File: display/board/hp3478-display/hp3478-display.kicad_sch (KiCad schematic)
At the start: 2 parts, among them U1 PIC16F152xx-x_MP, U2 PIC16F152xx-x_PT

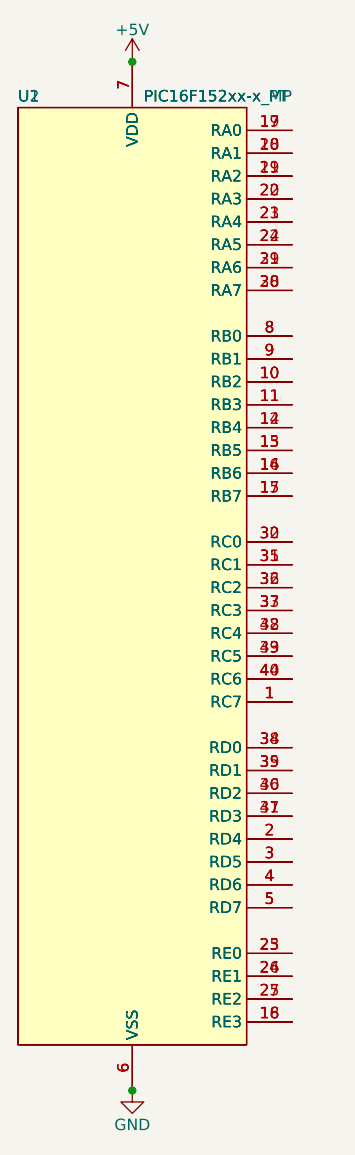
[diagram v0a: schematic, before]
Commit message: Clean up DNP alternate footprint for PIC.
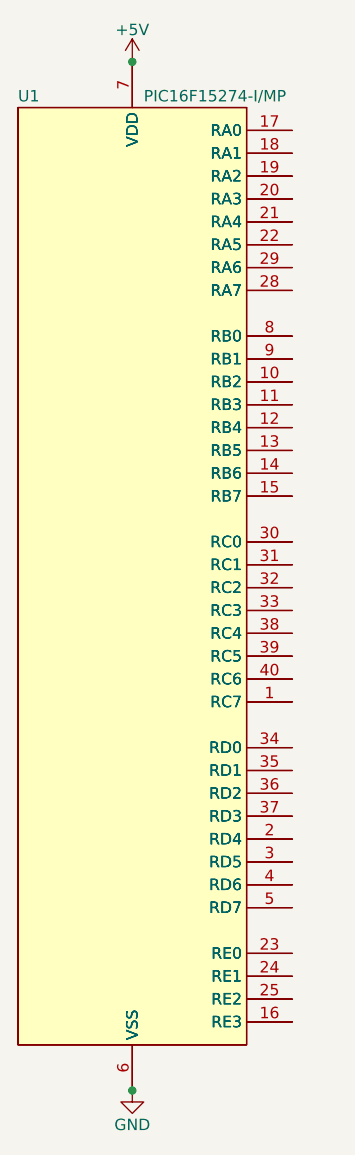
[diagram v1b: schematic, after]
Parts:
- U1: value PIC16F152xx-x_MP -> PIC16F15274-I/MP
- U2: value PIC16F152xx-x_PT -> DNP; now left out of the parts list
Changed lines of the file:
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@@
   )
   (symbol (lib_id "0Local:PIC16F152xx-x_PT") (at 40.64 130.81 0) (unit 1)
-    (in_bom yes) (on_board yes)
+    (in_bom no) (on_board yes)
     (property "Reference" "U2" (id 0) (at 27.94 83.82 0)
-      (effects (font (size 1.27 1.27)) (justify left))
+      (effects (font (size 1.27 1.27)) (justify left) hide)
     )
-    (property "Value" "PIC16F152xx-x_PT" (id 1) (at 41.91 83.82 0)
-      (effects (font (size 1.27 1.27)) (justify left))
+    (property "Value" "DNP" (id 1) (at 41.91 83.82 0)
+      (effects (font (size 1.27 1.27)) (justify left) hide)
     )
     (property "Footprint" "Package_QFP:TQFP-44_10x10mm_P0.8mm" (id 2) (at 40.64 130.81 0)
@@
       (effects (font (size 1.27 1.27)) (justify left))
     )
-    (property "Value" "PIC16F152xx-x_MP" (id 1) (at 41.91 83.82 0)
+    (property "Value" "PIC16F15274-I/MP" (id 1) (at 41.91 83.82 0)
       (effects (font (size 1.27 1.27)) (justify left))
     )
@@
     )
     (path "/84f97309-c012-475a-8346-a323e5986003"
-      (reference "U1") (unit 1) (value "PIC16F152xx-x_MP") (footprint "Package_DFN_QFN:QFN-40-1EP_5x5mm_P0.4mm_EP3.8x3.8mm_ThermalVias")
+      (reference "U1") (unit 1) (value "PIC16F15274-I/MP") (footprint "Package_DFN_QFN:QFN-40-1EP_5x5mm_P0.4mm_EP3.8x3.8mm_ThermalVias")
     )
     (path "/344cc245-2c6a-4a04-b559-c2e8c4d256b6"
-      (reference "U2") (unit 1) (value "PIC16F152xx-x_PT") (footprint "Package_QFP:TQFP-44_10x10mm_P0.8mm")
+      (reference "U2") (unit 1) (value "DNP") (footprint "Package_QFP:TQFP-44_10x10mm_P0.8mm")
     )
   )

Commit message: Assign all pins.
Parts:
- added C1: 22u, Capacitor_SMD:C_1206_3216Metric, symbol Device:C
- added C2, C3: 100n, Capacitor_SMD:C_0603_1608Metric, symbol Device:C
- added J1: SFV10R-1ST, 0Local:Amphenol_SFV10R-1ST, symbol Connector_Generic:Conn_01x10
- added J2: DNP, Connector_PinHeader_2.54mm:PinHeader_1x06_P2.54mm_Vertical, symbol Connector_Generic:Conn_01x06
- added R10, R11, R12, R13, R14, R15, R16, R17, R18, R19, R20, R21, R22, R23, R24, R25, R26: R, Resistor_SMD:R_0603_1608Metric, symbol Device:R
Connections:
- net +5V: now also C1.1, C2.1, C3.1, J1.1 (Pin_1), J1.2 (Pin_2), J2.2 (Pin_2)
- net GND: now also C1.2, C2.2, C3.2, J1.10 (Pin_10), J1.3 (Pin_3), J1.4 (Pin_4), J2.3 (Pin_3)
- net HA7: now reaches U1.1 (RC7), U2.1 (RC7)
- net HA7: now also R17.1
- net K8: now reaches U1.10 (RB2), U2.10 (RB2)
- net P1: now reaches U1.12 (RB4), U2.14 (RB4)
- net SYNC: now reaches U1.13 (RB5), U2.15 (RB5)
- net PGC/ISA: now reaches U1.14 (ICSPCLK/RB6), U2.16 (ICSPCLK/RB6)
- net PGC/ISA: now also J2.5 (Pin_5)
- net PGD/IWA: now reaches U1.15 (ICSPDAT/RB7), U2.17 (ICSPDAT/RB7)
- net PGD/IWA: now also J2.4 (Pin_4)
- net ~{MCLR}: now reaches U1.16 (~{MCLR}/RE3), U2.18 (~{MCLR}/RE3)
- net ~{MCLR}: now also J2.1 (Pin_1)
- net PWO: now reaches U1.17 (RA0), U2.19 (RA0)
- net HA12: now reaches U1.2 (RD4), U2.2 (RD4)
- net HA12: now also R22.1
- net K0: now reaches U1.18 (RA1), U2.20 (RA1)
- net K1: now reaches U1.19 (RA2), U2.21 (RA2)
- net K2: now reaches U1.20 (VREF/RA3), U2.22 (VREF/RA3)
- net K3: now reaches U1.21 (RA4), U2.23 (RA4)
- net K4: now reaches U1.22 (RA5), U2.24 (RA5)
- net K9: now reaches U1.23 (RE0), U2.25 (RE0)
- net K10: now reaches U1.24 (RE1), U2.26 (RE1)
- net K11: now reaches U1.25 (RE2), U2.27 (RE2)
- net HA13: now reaches U1.3 (RD5), U2.3 (RD5)
- net HA13: now also R23.1
- net K6: now reaches U1.28 (CLKIN/RA7), U2.30 (CLKIN/RA7)
- net K5: now reaches U1.29 (CLKOUT/RA6), U2.31 (CLKOUT/RA6)
- net HA0: now reaches U1.30 (RC0), U2.32 (RC0)
- net HA0: now also R10.1
- net HA1: now reaches U1.31 (RC1), U2.35 (RC1)
- net HA1: now also R11.1
- net HA2: now reaches U1.32 (RC2), U2.36 (RC2)
- net HA2: now also R12.1
- net HA3: now reaches U1.33 (RC3), U2.37 (RC3)
- net HA3: now also R13.1
- net HA8: now reaches U1.34 (RD0), U2.38 (RD0)
- net HA8: now also R18.1
- net HA9: now reaches U1.35 (RD1), U2.39 (RD1)
- net HA9: now also R19.1
- net HA14: now reaches U1.4 (RD6), U2.4 (RD6)
- net HA14: now also R24.1
- net HA10: now reaches U1.36 (RD2), U2.40 (RD2)
- net HA10: now also R20.1
- net HA11: now reaches U1.37 (RD3), U2.41 (RD3)
- net HA11: now also R21.1
- net HA4: now reaches U1.38 (RC4), U2.42 (RC4)
- net HA4: now also R14.1
- net HA5: now reaches U1.39 (RC5), U2.43 (RC5)
- net HA5: now also R15.1
- net HA6: now reaches U1.40 (RC6), U2.44 (RC6)
- net HA6: now also R16.1
- net HA15: now reaches U1.5 (RD7), U2.5 (RD7)
- net HA15: now also R25.1
- net HA16: now reaches U1.8 (RB0), U2.8 (RB0)
- net HA16: now also R26.1
- net K7: now reaches U1.9 (RB1), U2.9 (RB1)
- new net A0: R10.2
- new net A1: R11.2
- new net A10: R20.2
- new net A11: R21.2
- new net A12: R22.2
- new net A13: R23.2
- new net A14: R24.2
- new net A15: R25.2
- new net A16: R26.2
- new net A2: R12.2
- new net A3: R13.2
- new net A4: R14.2
- new net A5: R15.2
- new net A6: R16.2
- new net A7: R17.2
- new net A8: R18.2
- new net A9: R19.2
- no-connect marks 0 -> 1

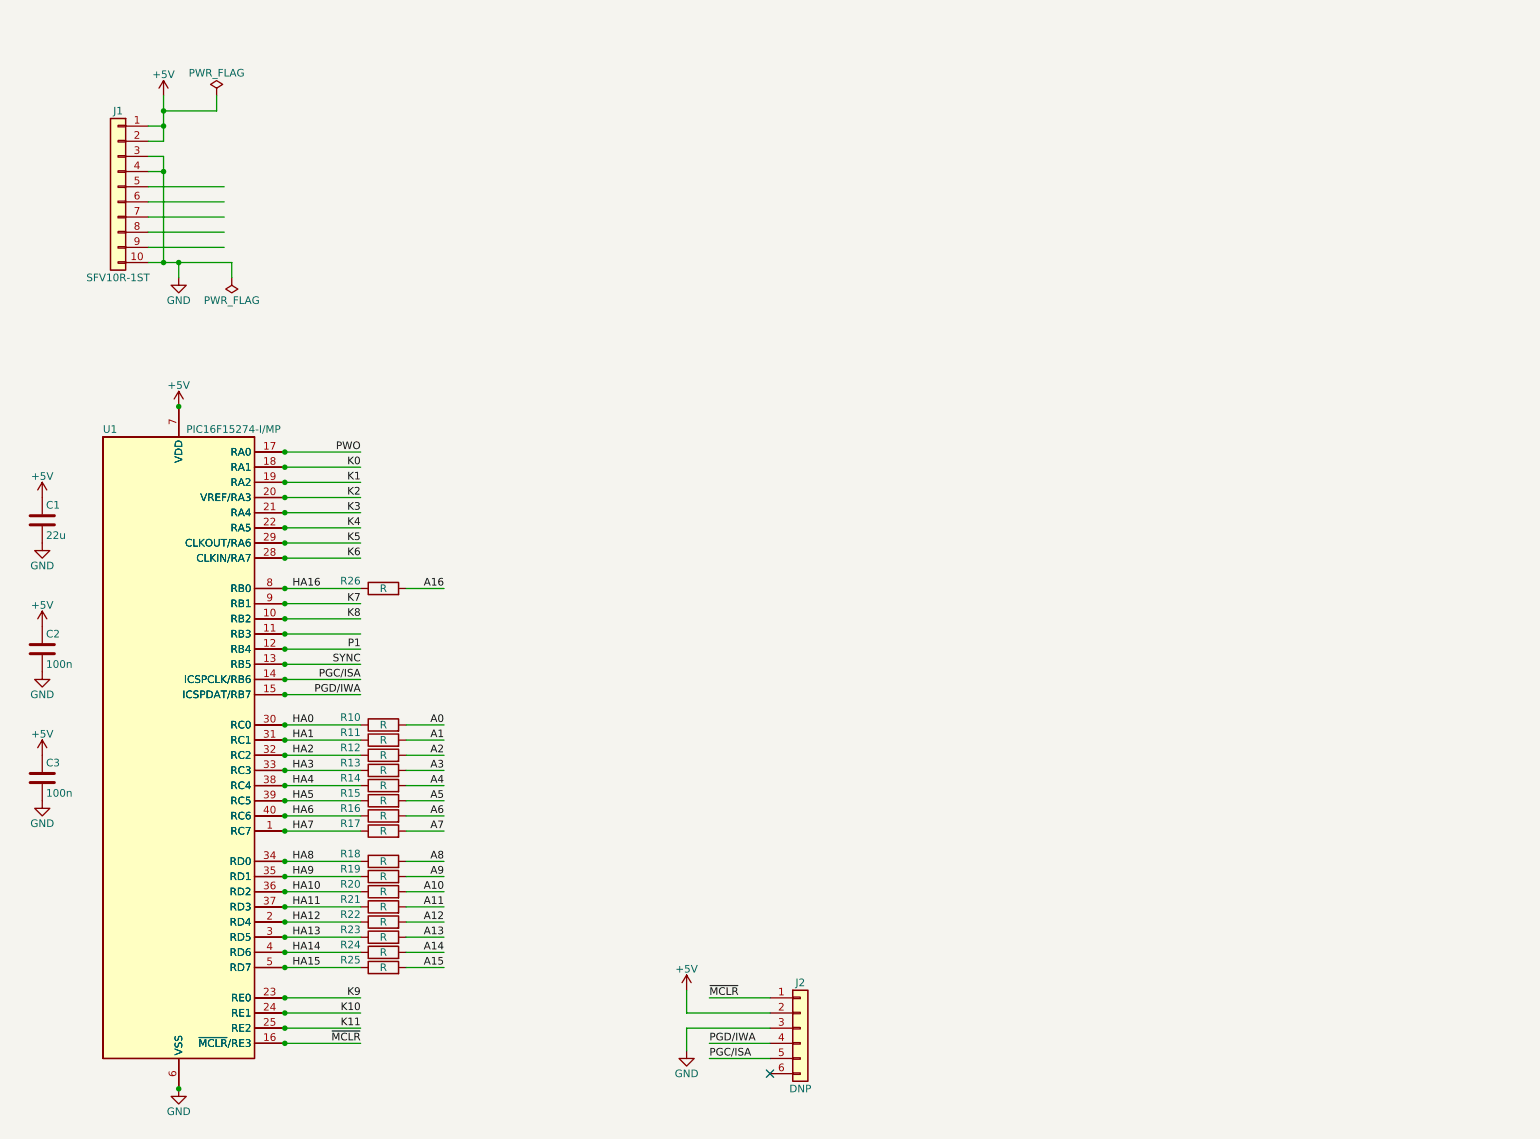
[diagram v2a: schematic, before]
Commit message: Add digits to board.
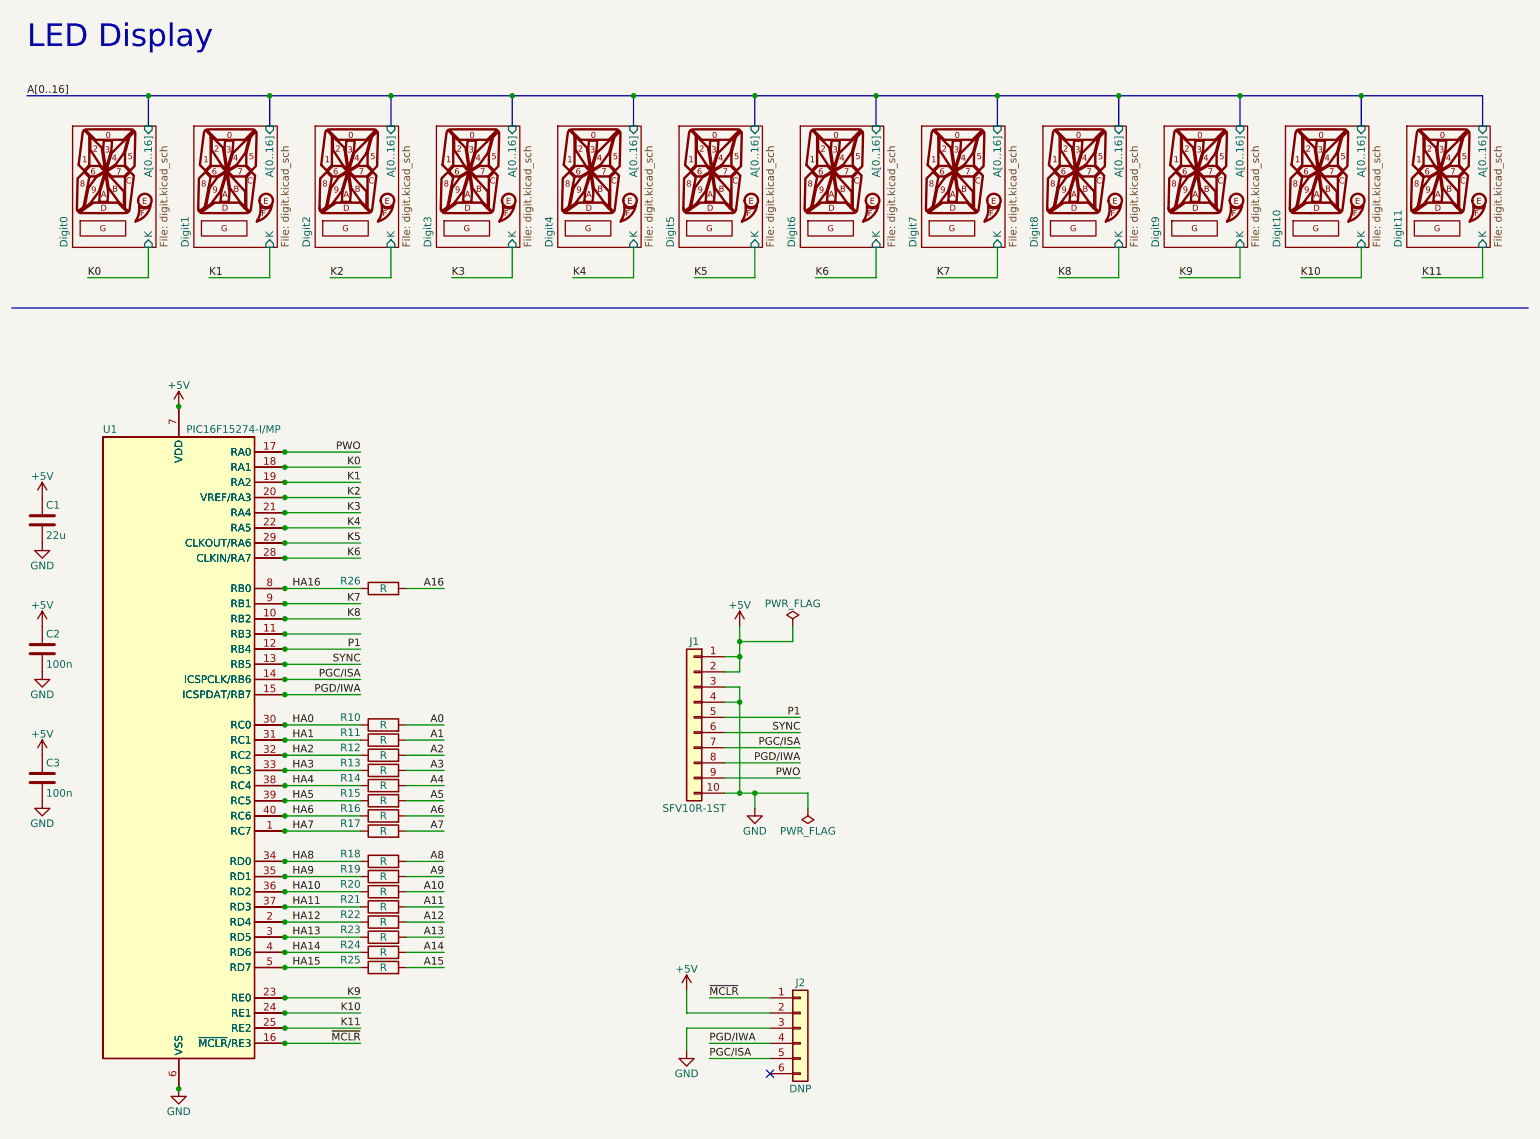
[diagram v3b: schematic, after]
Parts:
- U1: footprint Package_DFN_QFN:QFN-40-1EP_5x5mm_P0.4mm_EP3.8x3.8mm_ThermalVias -> Package_DFN_QFN:QFN-40-1EP_5x5mm_P0.4mm_EP3.8x3.8mm
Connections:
- net P1: now also J1.5 (Pin_5)
- net PGC/ISA: now also J1.7 (Pin_7)
- net PGD/IWA: now also J1.8 (Pin_8)
- net PWO: now also J1.9 (Pin_9)
- net SYNC: now also J1.6 (Pin_6)
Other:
- added sheet Digit0 (digit.kicad_sch)
- added sheet Digit1 (digit.kicad_sch)
- added sheet Digit10 (digit.kicad_sch)
- added sheet Digit11 (digit.kicad_sch)
- added sheet Digit2 (digit.kicad_sch)
- added sheet Digit3 (digit.kicad_sch)
- added sheet Digit4 (digit.kicad_sch)
- added sheet Digit5 (digit.kicad_sch)
- added sheet Digit6 (digit.kicad_sch)
- added sheet Digit7 (digit.kicad_sch)
- added sheet Digit8 (digit.kicad_sch)
- added sheet Digit9 (digit.kicad_sch)
- note added: "LED Display"
- moved on the sheet: J1

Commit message: Reorganize schematic.
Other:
- note added: "Current Limit"
- note added: "ICSP"
- note added: "Input"
- note added: "MCU"
- moved on the sheet: C1, C2, C3, J1, J2, R10, R11, R12, R13, R14, R15, R16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

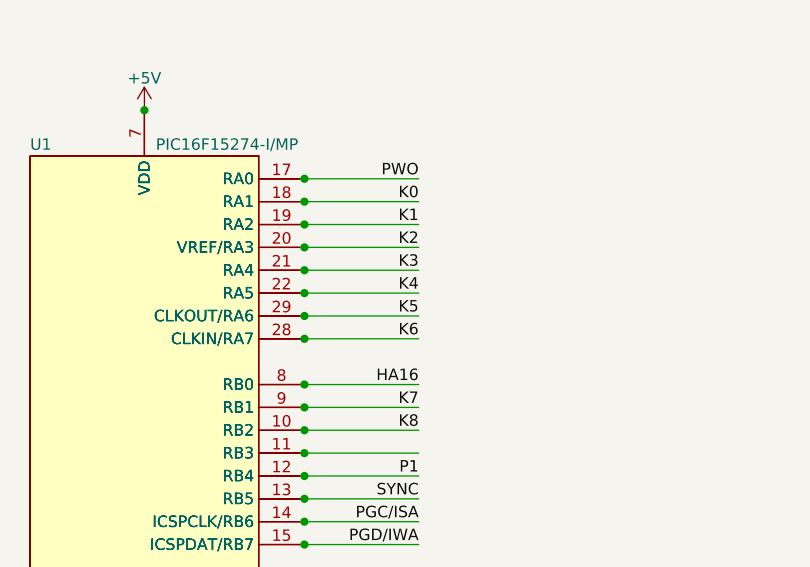
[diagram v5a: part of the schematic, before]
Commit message: Route LED anode bus.
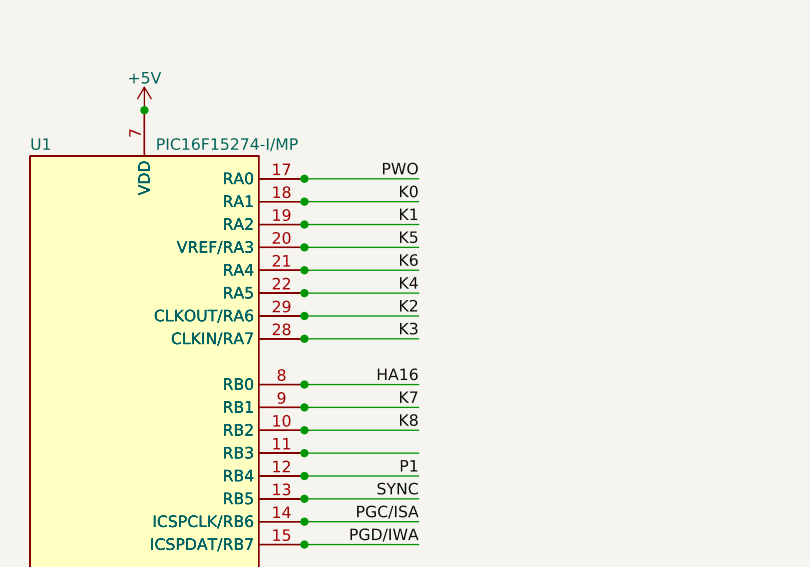
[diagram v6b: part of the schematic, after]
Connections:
- net K2: now also U1.29 (CLKOUT/RA6), U2.31 (CLKOUT/RA6); no longer U1.20 (VREF/RA3), U2.22 (VREF/RA3)
- net K3: now also U1.28 (CLKIN/RA7), U2.30 (CLKIN/RA7); no longer U1.21 (RA4), U2.23 (RA4)
- net K5: now also U1.20 (VREF/RA3), U2.22 (VREF/RA3); no longer U1.29 (CLKOUT/RA6), U2.31 (CLKOUT/RA6)
- net K6: now also U1.21 (RA4), U2.23 (RA4); no longer U1.28 (CLKIN/RA7), U2.30 (CLKIN/RA7)
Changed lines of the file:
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@@
     (effects (font (size 3.81 3.81)) (justify left bottom))
   )
-  (label "K6" (at 144.78 106.68 180)
+  (label "K6" (at 144.78 99.06 180)
     (effects (font (size 1.27 1.27)) (justify right bottom))
   )
@@
     (effects (font (size 1.27 1.27)) (justify left bottom))
   )
-  (label "K2" (at 144.78 96.52 180)
+  (label "K2" (at 144.78 104.14 180)
     (effects (font (size 1.27 1.27)) (justify right bottom))
   )
@@
     (effects (font (size 1.27 1.27)) (justify left bottom))
   )
-  (label "K5" (at 144.78 104.14 180)
+  (label "K5" (at 144.78 96.52 180)
     (effects (font (size 1.27 1.27)) (justify right bottom))
   )
@@
     (effects (font (size 1.27 1.27)) (justify right bottom))
   )
-  (label "K3" (at 144.78 99.06 180)
+  (label "K3" (at 144.78 106.68 180)
     (effects (font (size 1.27 1.27)) (justify right bottom))
   )
